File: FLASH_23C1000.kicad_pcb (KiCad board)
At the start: 2 copper layers, 16.5 x 39.4 mm, 9 parts, among them J1 uPD23C1000 / FLASH, U1 29F010 TSOP-32 20mm, U2 29F010 sTSOP-32 14mm, U3 29F010 PLCC 7x9

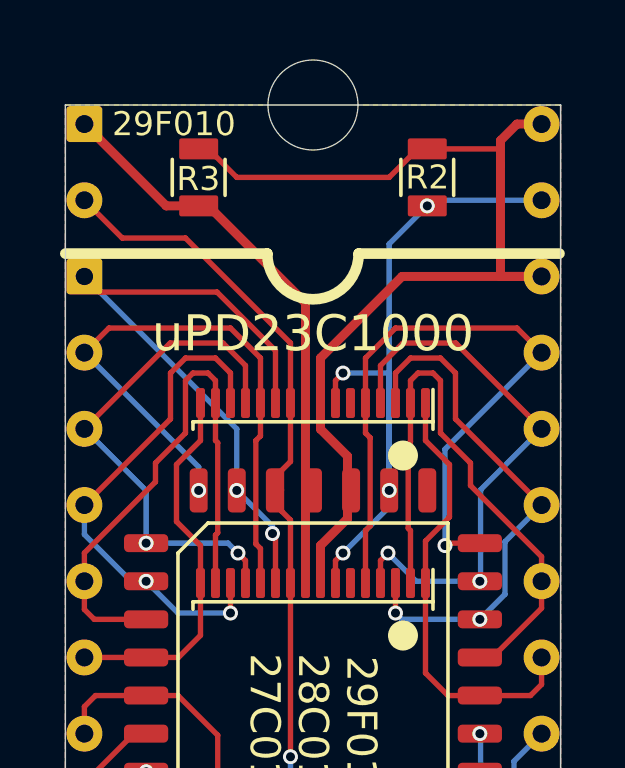
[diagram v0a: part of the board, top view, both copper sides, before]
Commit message: Rename FlashROM_8300 to FLASH_23C1000
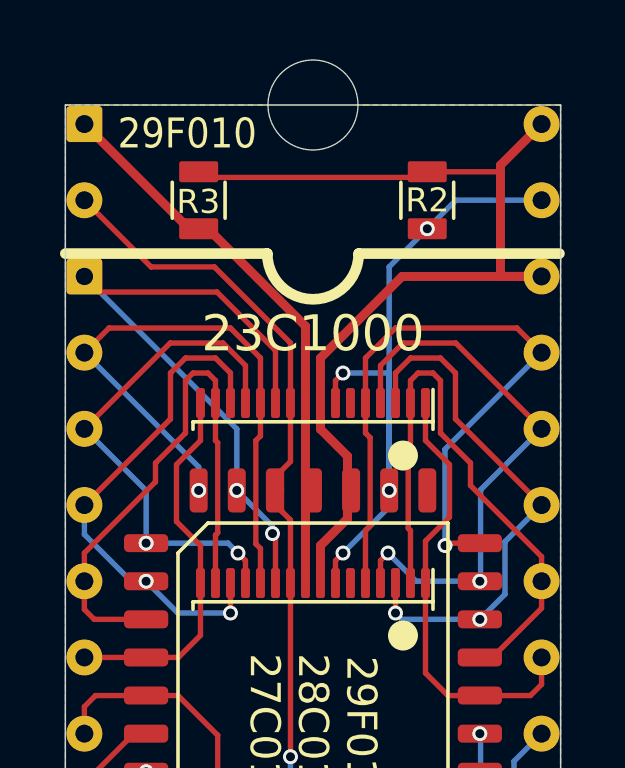
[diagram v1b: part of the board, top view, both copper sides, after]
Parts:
- moved R2 0.76 mm to (153.8, 81.0)
- moved R3 0.76 mm to (146.2, 81.0)
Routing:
- net /VCC: track 35.3 -> 34.0 mm
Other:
- board text added: "23C1000"
- board text added: "github.com/bkw777/aDIPters"
- board text removed: "http://tandy.wiki/FlashROM_8300"
- board text removed: "uPD23C1000"

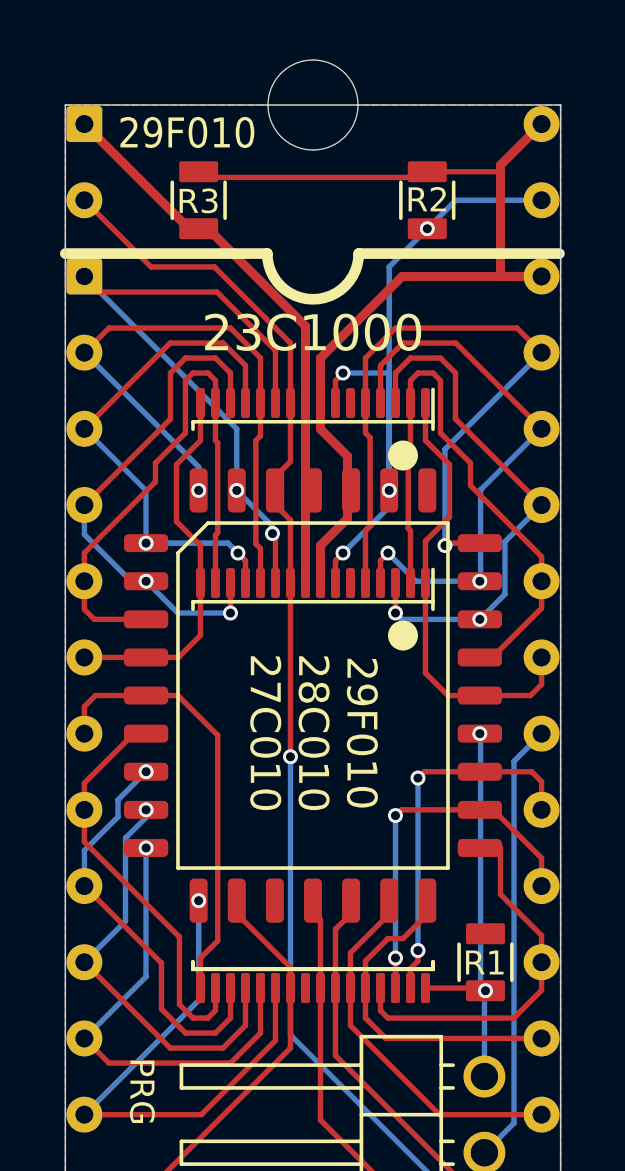
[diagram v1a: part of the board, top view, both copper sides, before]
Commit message: add model 100 optrom programming adapter. readme and renders
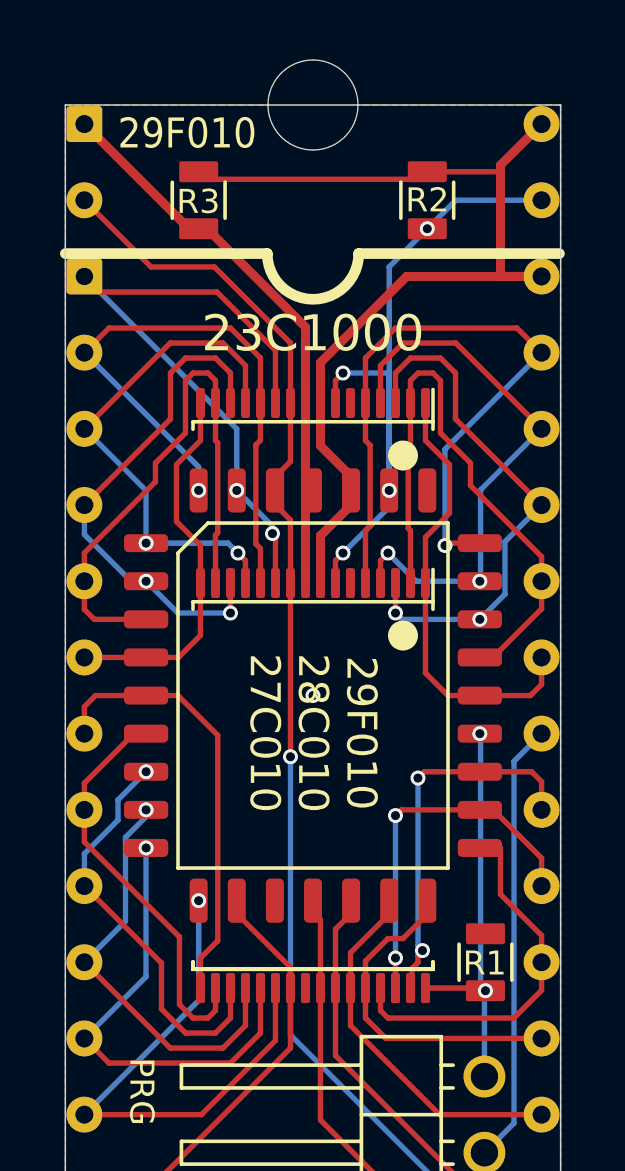
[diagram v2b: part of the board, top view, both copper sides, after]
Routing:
- net /GND: vias 0 -> 1

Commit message: kicad 6
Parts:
- J1: value uPD23C1000 / FLASH -> 23C1000 / 29F010 switchable pinout; footprint 000_LOCAL:DIP32_0.6_pcb_sil_pins -> 000_LOCAL:DIP32_DIP28_0.6_pcb_sil_pins
- moved JP1 0.25 mm to (155.5, 115.2)
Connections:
- net /A16_~OE renamed /A16_~{OE}
- net /~CE renamed /~{CE}
- net /~OE renamed /~{OE}
- net /~WE renamed /~{WE}
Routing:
- net /GND: track 0.00 -> 3.56 mm
- net /A3: track 14.7 -> 13.8 mm
- net /A11: track 14.9 -> 14.0 mm
- net /A5: track 19.2 -> 18.7 mm
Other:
- net class Default removed

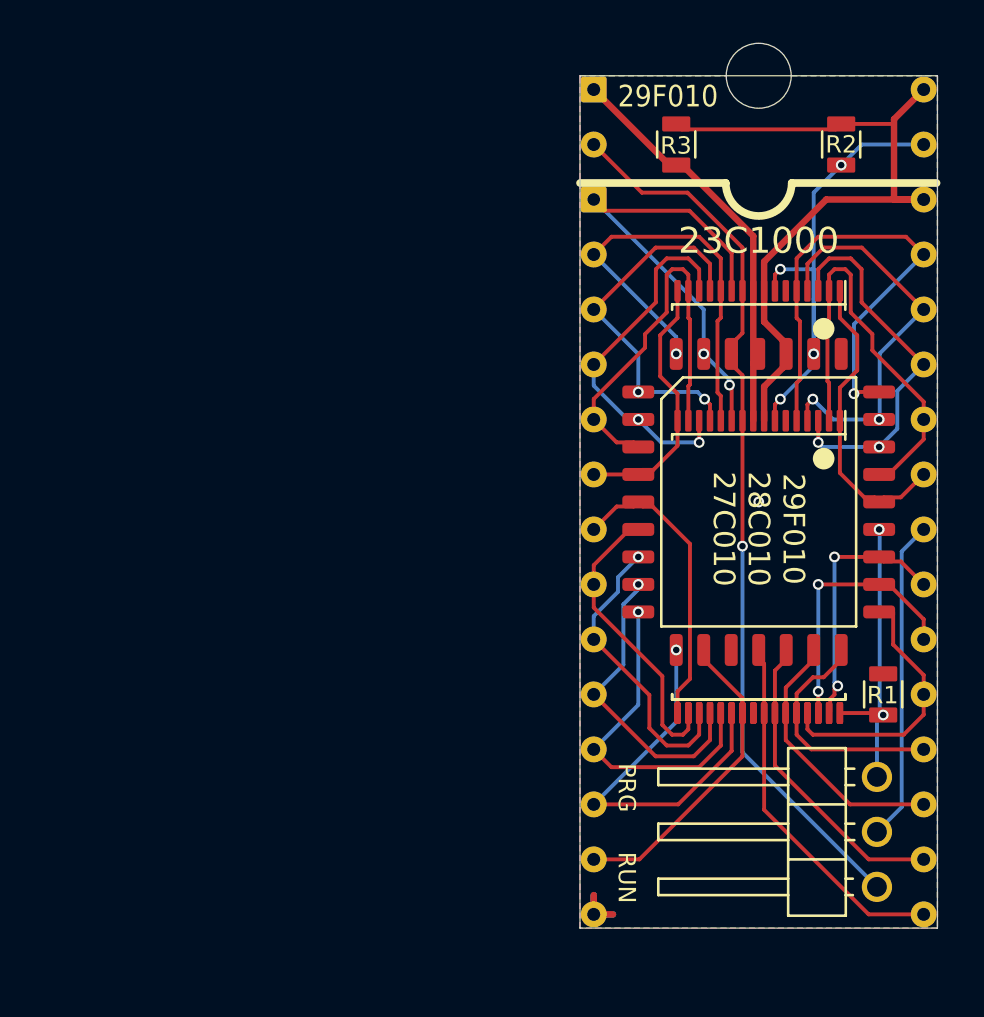
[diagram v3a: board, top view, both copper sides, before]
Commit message: Fix wrong pinout on FlashROM_100 TSOPgit add -A!
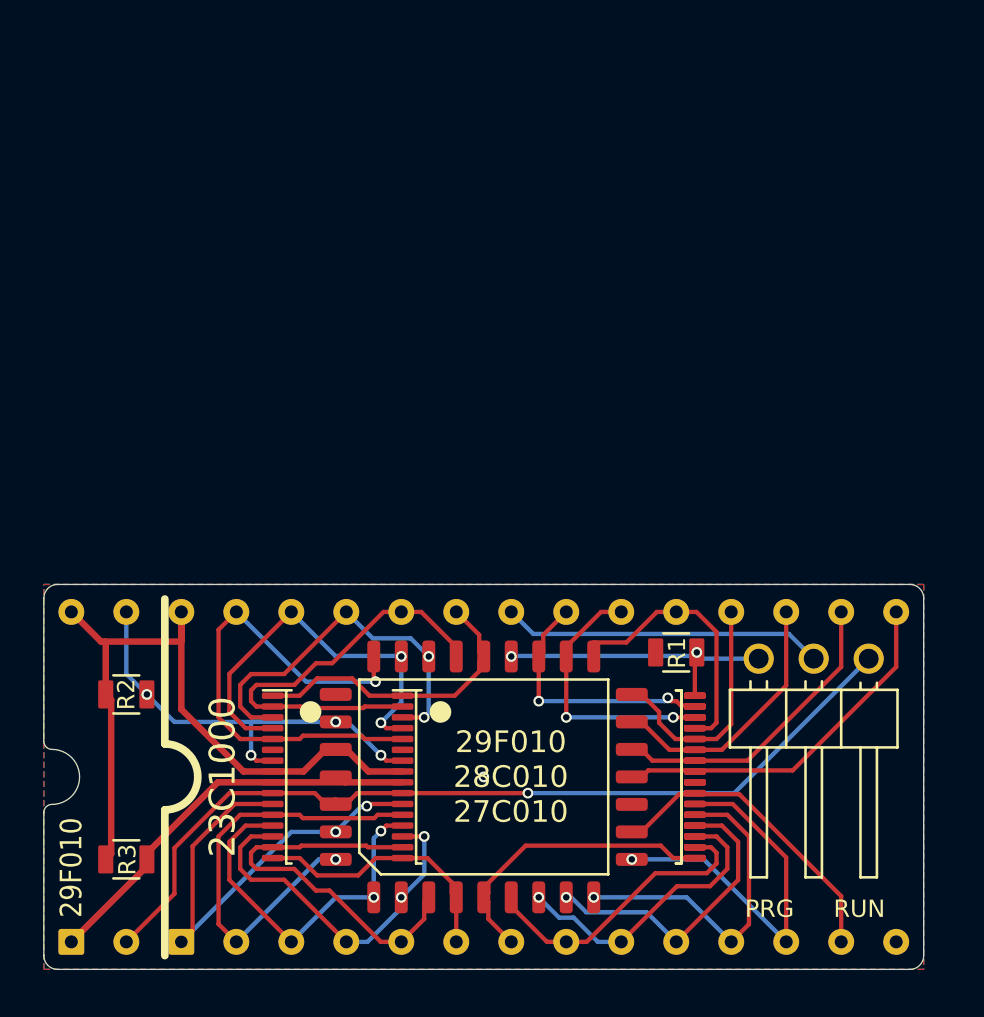
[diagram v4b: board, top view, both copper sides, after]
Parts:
- removed REF**: NPTH_3mm, 000_LOCAL:NPTH_3mm
- moved R2 41.7 mm to (120.8, 106.3), turned to 180 degrees
- moved R3 41.7 mm to (120.8, 114.0), turned to 180 degrees
- moved J1 18.0 mm to (137.3, 110.2), turned to 90 degrees
- moved U1 18.0 mm to (137.3, 110.2), turned to -90 degrees
- moved U3 18.0 mm to (137.3, 110.2), turned to 90 degrees
- moved U2 13.7 mm to (140.3, 110.2), turned to -90 degrees
- moved JP1 10.5 mm to (155.1, 104.7), turned to -90 degrees
- moved R1 9.75 mm to (146.2, 104.4), turned to 180 degrees
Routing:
- net /GND: track 3.56 -> 0.00 mm
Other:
- board size 16.5 x 39.4 mm -> 40.6 x 17.8 mm
- board text added: "${COMMENT1} ${TITLE} ${REVISION}"
- board text added: "R1,R2: ${00000000-0000-0000-0000-00005e638d11:VALUE} Legs: TE 1544210"
- board text removed: "Legs: TE 1544210"
- board text removed: "Move the jumper from RUN to PRG"
- board text removed: "Place board in programmer ZIF socket"
- board text removed: "R1, R2: 47k"
- board text removed: "To program:"
- board text removed: "github.com/bkw777/aDIPters"

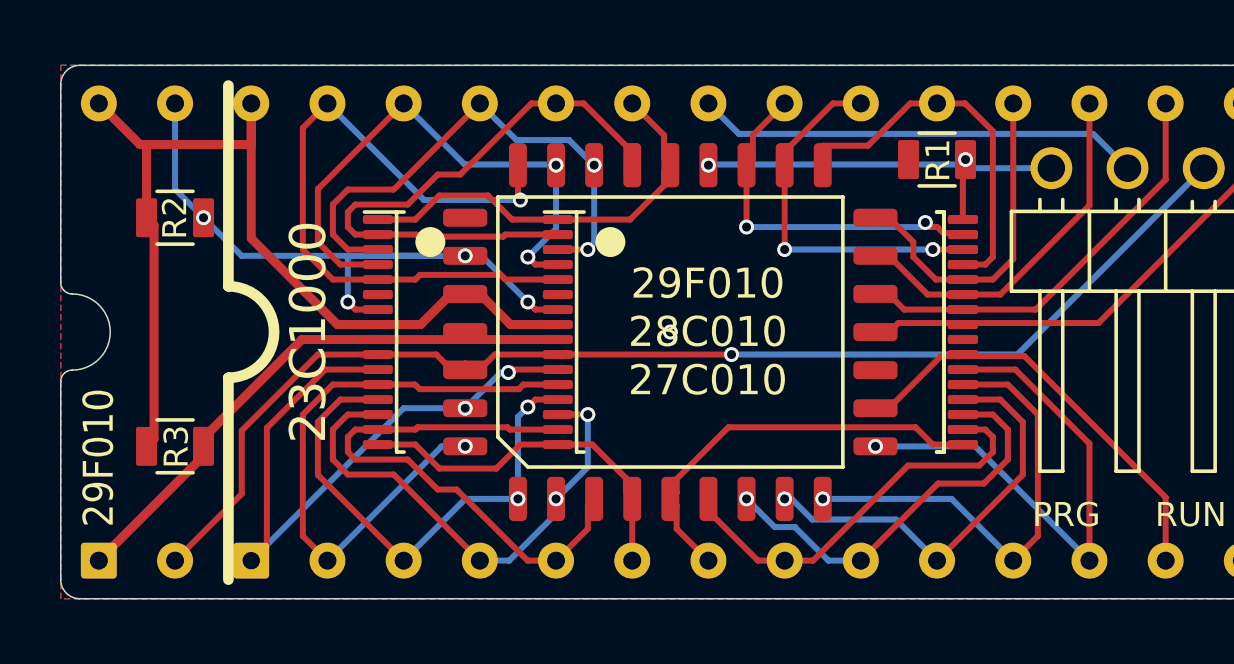
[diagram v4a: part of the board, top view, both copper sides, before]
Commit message: 23C1000 silk, sch, gnd
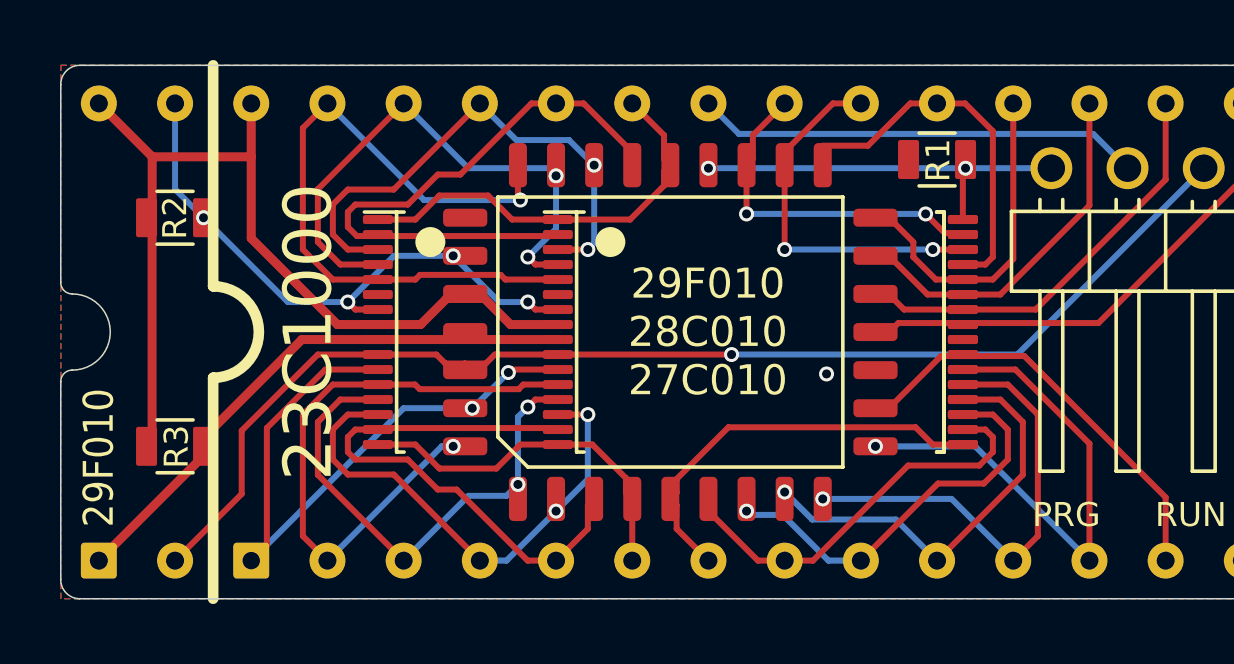
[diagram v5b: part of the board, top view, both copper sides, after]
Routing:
- net /~{WE}: track 23.8 -> 19.7 mm
- net /VCC: track 33.9 -> 32.3 mm

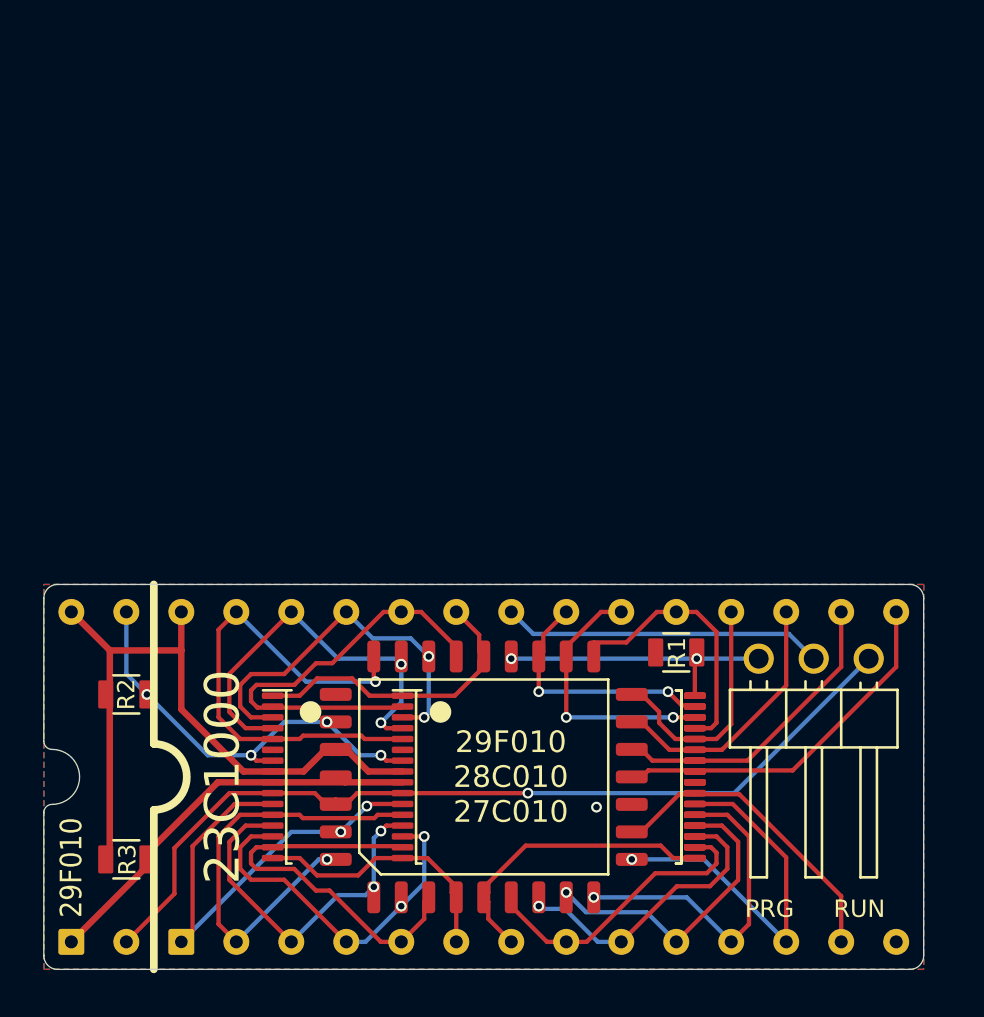
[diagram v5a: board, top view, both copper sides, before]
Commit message: dual-tsop footprint on flash_23c1000
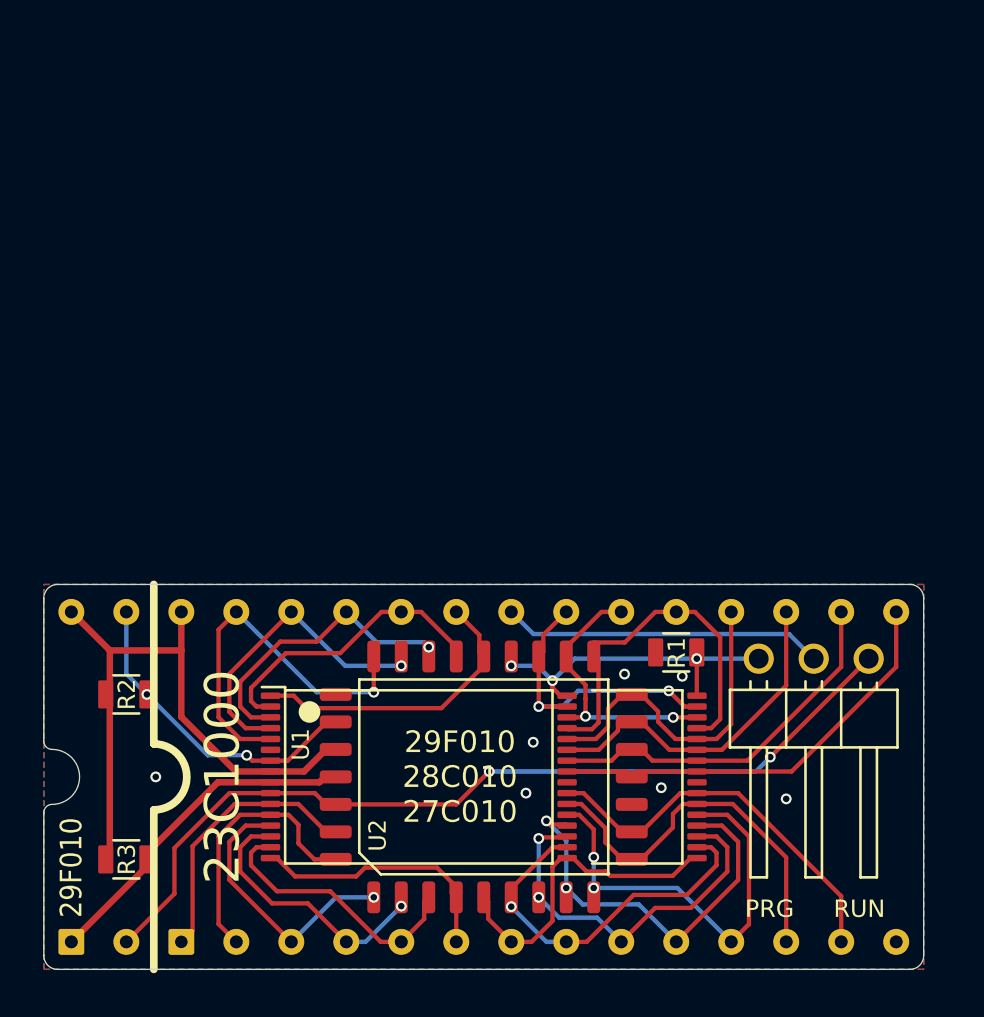
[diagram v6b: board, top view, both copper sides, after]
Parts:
- removed the U2 at (140.3, 110.2)
- U1: value 29F010 TSOP-32 20mm -> 29F010 TSOP-32; footprint 000_LOCAL:TSOP32-20mm -> 000_LOCAL:TSOP32-dual
- turned U1 to 0 degrees
- renumbered U3 to U2
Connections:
- net /GND renamed GND
- net /VCC renamed VCC
- U1 pad 6: (no net) -> unconnected-(U1-NC-Pad6)
- U2 pad 30: (no net) -> unconnected-(U2-NC-Pad30)
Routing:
- net /A15: track 22.0 -> 12.6 mm, vias 2 -> 0
- net /A12: track 20.0 -> 12.4 mm, vias 1 -> 0
- net /A5: track 18.7 -> 12.6 mm
- net /A9: track 19.7 -> 13.7 mm
- net /A14: track 23.2 -> 17.6 mm
- net /D7: track 12.6 -> 17.3 mm
- net /~{WE}: track 19.7 -> 14.9 mm, vias 4 -> 2
- net /A6: track 16.9 -> 12.2 mm, vias 2 -> 1
- net /A0: track 14.1 -> 18.6 mm, vias 1 -> 2
- net /D6: track 11.2 -> 15.5 mm
- net /D0: track 15.3 -> 19.6 mm, vias 1 -> 2
- net /A13: track 18.4 -> 14.1 mm, vias 2 -> 1
- net /A1: track 13.5 -> 17.7 mm, vias 1 -> 2
- net /A7: track 16.8 -> 12.7 mm, vias 2 -> 1
- net /A2: track 13.7 -> 17.4 mm, vias 0 -> 1
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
